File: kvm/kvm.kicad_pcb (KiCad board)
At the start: 2 copper layers, 3 parts, among them U1 FSUSB42MUX, U2 LTC4412xS6, U4 L78L33_SOT89

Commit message: finished schematic
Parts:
- added C1: 100n, Capacitor_SMD:C_0603_1608Metric_Pad1.08x0.95mm_HandSolder, F.Cu at (158.6, 75.0)
- added C10: 100u, Capacitor_THT:CP_Radial_D5.0mm_P2.00mm, F.Cu at (95.9, 17.8)
- added C11: 100u, Capacitor_THT:CP_Radial_D5.0mm_P2.00mm, F.Cu at (103.6, 17.8)
- added C12: 100u, Capacitor_THT:CP_Radial_D5.0mm_P2.00mm, F.Cu at (88.3, 17.8)
- added C13: 100n, Capacitor_SMD:C_0603_1608Metric_Pad1.08x0.95mm_HandSolder, F.Cu at (152.1, 82.7)
- added C14: 100n, Capacitor_SMD:C_0603_1608Metric_Pad1.08x0.95mm_HandSolder, F.Cu at (172.0, 56.0)
- added C15: 100n, Capacitor_SMD:C_0603_1608Metric_Pad1.08x0.95mm_HandSolder, F.Cu at (141.8, 82.9)
- added C16: 100n, Capacitor_SMD:C_0603_1608Metric_Pad1.08x0.95mm_HandSolder, F.Cu at (168.4, 65.9)
- added C17: 100n, Capacitor_SMD:C_0603_1608Metric_Pad1.08x0.95mm_HandSolder, F.Cu at (150.6, 87.8)
- added C18: 100n, Capacitor_SMD:C_0603_1608Metric_Pad1.08x0.95mm_HandSolder, F.Cu at (180.7, 54.4)
- added C19: 100n, Capacitor_SMD:C_0603_1608Metric_Pad1.08x0.95mm_HandSolder, F.Cu at (146.3, 87.8)
- added C2: 100u, Capacitor_THT:CP_Radial_D5.0mm_P2.00mm, F.Cu at (70.5, 17.8)
- added C20: 100n, Capacitor_SMD:C_0603_1608Metric_Pad1.08x0.95mm_HandSolder, F.Cu at (172.0, 58.5)
- added C21: 10u, Capacitor_SMD:C_0805_2012Metric_Pad1.18x1.45mm_HandSolder, F.Cu at (167.1, 60.7)
- added C3: 100n, Capacitor_SMD:C_0603_1608Metric_Pad1.08x0.95mm_HandSolder, F.Cu at (147.8, 82.7)
- added C4: 100n, Capacitor_SMD:C_0603_1608Metric_Pad1.08x0.95mm_HandSolder, F.Cu at (164.0, 65.9)
- added C5: 100n, Capacitor_SMD:C_0603_1608Metric_Pad1.08x0.95mm_HandSolder, F.Cu at (158.6, 72.5)
- added C6: 33p, Capacitor_SMD:C_0603_1608Metric_Pad1.08x0.95mm_HandSolder, F.Cu at (179.7, 49.4)
- added C7: 33p, Capacitor_SMD:C_0603_1608Metric_Pad1.08x0.95mm_HandSolder, F.Cu at (168.4, 63.4)
- added C8: 100n, Capacitor_SMD:C_0603_1608Metric_Pad1.08x0.95mm_HandSolder, F.Cu at (146.3, 85.2)
- added C9: 100u, Capacitor_THT:CP_Radial_D5.0mm_P2.00mm, F.Cu at (78.7, 17.8)
- added D1: D_Schottky, Diode_SMD:D_SOD-123F, F.Cu at (165.1, 48.3)
- added D2: LED, LED_SMD:LED_0805_2012Metric_Pad1.15x1.40mm_HandSolder, F.Cu at (156.5, 48.3)
- added F1: Polyfuse, Fuse:Fuse_1206_3216Metric_Pad1.42x1.75mm_HandSolder, F.Cu at (142.6, 80.0)
- added F2: Polyfuse, Fuse:Fuse_1206_3216Metric_Pad1.42x1.75mm_HandSolder, F.Cu at (136.0, 86.5)
- added F3: Polyfuse, Fuse:Fuse_1206_3216Metric_Pad1.42x1.75mm_HandSolder, F.Cu at (158.9, 61.9)
- added F4: Polyfuse, Fuse:Fuse_1206_3216Metric_Pad1.42x1.75mm_HandSolder, F.Cu at (158.9, 65.2)
- added J1: USB_C_Receptacle_USB2.0, Connector_USB:USB_C_Receptacle_GCT_USB4085, F.Cu at (95.0, 89.0)
- added J2: USB_C_Receptacle_USB2.0, Connector_USB:USB_C_Receptacle_GCT_USB4085, F.Cu at (95.0, 102.0)
- added J3: USB_A_Stacked, Connector_USB:USB_A_Wuerth_61400826021_Horizontal_Stacked, F.Cu at (32.3, 67.6)
- added J4: USB_A_Stacked, Connector_USB:USB_A_Wuerth_61400826021_Horizontal_Stacked, F.Cu at (32.1, 87.1)
- added L1: 600, Resistor_SMD:R_0603_1608Metric_Pad0.98x0.95mm_HandSolder, F.Cu at (168.1, 68.5)
- added L2: 600, Resistor_SMD:R_0603_1608Metric_Pad0.98x0.95mm_HandSolder, F.Cu at (152.1, 80.2)
- added L3: 600, Resistor_SMD:R_0603_1608Metric_Pad0.98x0.95mm_HandSolder, F.Cu at (162.6, 81.3)
- added L4: 600, Resistor_SMD:R_0603_1608Metric_Pad0.98x0.95mm_HandSolder, F.Cu at (179.7, 51.9)
- added L5: 600, Resistor_SMD:R_0603_1608Metric_Pad0.98x0.95mm_HandSolder, F.Cu at (150.6, 85.2)
- added L6: 600, Resistor_SMD:R_0603_1608Metric_Pad0.98x0.95mm_HandSolder, F.Cu at (184.0, 49.4)
- added L7: 600, Resistor_SMD:R_0603_1608Metric_Pad0.98x0.95mm_HandSolder, F.Cu at (163.7, 68.5)
- added Q1: Q_PMOS_GSD, Package_TO_SOT_SMD:SOT-23-3, F.Cu at (50.8, 30.5)
- added R1: 1M, Resistor_SMD:R_0603_1608Metric_Pad0.98x0.95mm_HandSolder, F.Cu at (176.3, 58.3)
- added R10: 10K, Resistor_SMD:R_0603_1608Metric_Pad0.98x0.95mm_HandSolder, F.Cu at (172.7, 61.0)
- added R11: 47K, Resistor_SMD:R_0603_1608Metric_Pad0.98x0.95mm_HandSolder, F.Cu at (162.9, 73.5)
- added R12: 100k, Resistor_SMD:R_0603_1608Metric_Pad0.98x0.95mm_HandSolder, F.Cu at (147.8, 80.2)
- added R13: 780, Resistor_SMD:R_0603_1608Metric_Pad0.98x0.95mm_HandSolder, F.Cu at (147.8, 77.7)
- added R14: 470K, Resistor_SMD:R_0603_1608Metric_Pad0.98x0.95mm_HandSolder, F.Cu at (188.0, 58.4)
- added R2: 1M, Resistor_SMD:R_0603_1608Metric_Pad0.98x0.95mm_HandSolder, F.Cu at (172.7, 63.5)
- added R3: 5.11K, Resistor_SMD:R_0603_1608Metric_Pad0.98x0.95mm_HandSolder, F.Cu at (176.3, 55.8)
- added R4: 5.11K, Resistor_SMD:R_0603_1608Metric_Pad0.98x0.95mm_HandSolder, F.Cu at (163.7, 71.0)
- added R5: 5.11K, Resistor_SMD:R_0603_1608Metric_Pad0.98x0.95mm_HandSolder, F.Cu at (152.1, 77.7)
- added R6: 5.11K, Resistor_SMD:R_0603_1608Metric_Pad0.98x0.95mm_HandSolder, F.Cu at (180.7, 57.0)
- added R7: 680, Resistor_SMD:R_0603_1608Metric_Pad0.98x0.95mm_HandSolder, F.Cu at (184.0, 51.9)
- added R8: 10K, Resistor_SMD:R_0603_1608Metric_Pad0.98x0.95mm_HandSolder, F.Cu at (164.0, 63.4)
- added R9: 20K, Resistor_SMD:R_0603_1608Metric_Pad0.98x0.95mm_HandSolder, F.Cu at (156.5, 80.0)
- added SW1: SW_DPDT_x2, Connector_PinHeader_2.54mm:PinHeader_1x03_P2.54mm_Vertical, F.Cu at (146.9, 62.5)
- added U3: GL850G, Package_SO:SSOP-28_5.3x10.2mm_P0.65mm, F.Cu at (43.2, 50.8)
- added U5: SRV05-4, Package_TO_SOT_SMD:SOT-23-6, F.Cu at (58.4, 38.1)
- added U6: SRV05-4, Package_TO_SOT_SMD:SOT-23-6, F.Cu at (41.8, 38.1)
- added Y1: Crystal, Library:ECS120184XCKM, F.Cu at (55.3, 20.3)
- U4: value L78L33_SOT89 -> SRV05-4; footprint Package_TO_SOT_SMD:SOT-89-3 -> Package_TO_SOT_SMD:SOT-23-6
- moved U2 41.2 mm to (70.7, 37.9)
- moved U4 38.1 mm to (50.8, 38.1)
- moved U1 38.1 mm to (83.8, 38.1)
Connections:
- U1 pad 1: unconnected-(U1-Pad1) -> V5
- U1 pad 10: unconnected-(U1-Pad10) -> GND
- U1 pad 2: unconnected-(U1-Pad2) -> Net-(SW1-Pad2)
- U1 pad 3: unconnected-(U1-Pad3) -> DP0
- U1 pad 4: unconnected-(U1-Pad4) -> DM0
- U1 pad 5: unconnected-(U1-Pad5) -> GND
- U1 pad 6: unconnected-(U1-Pad6) -> DM1IN
- U1 pad 7: unconnected-(U1-Pad7) -> DP1IN
- U1 pad 8: unconnected-(U1-Pad8) -> DM2IN
- U1 pad 9: unconnected-(U1-Pad9) -> DP2IN
- U2 pad 1: unconnected-(U2-Pad1) -> USB2V5
- U2 pad 2: unconnected-(U2-Pad2) -> GND
- U2 pad 3: unconnected-(U2-Pad3) -> GND
- U2 pad 4: unconnected-(U2-Pad4) -> Net-(U2-Pad4)
- U2 pad 5: unconnected-(U2-Pad5) -> /gate
- U2 pad 6: unconnected-(U2-Pad6) -> V5
- U4 pad 1: unconnected-(U4-Pad1) -> DP1
- U4 pad 2: unconnected-(U4-Pad2) -> GND
- U4 pad 3: unconnected-(U4-Pad3) -> DM1

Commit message: first layout version
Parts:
- moved L6 117.2 mm to (76.7, 96.7), turned to 180 degrees
- moved C18 114.3 mm to (76.8, 102.0), turned to -90 degrees
- moved C2 113.5 mm to (144.1, 104.2), turned to -90 degrees
- moved Q1 111.4 mm to (135.5, 102.9), turned to 90 degrees
- moved Y1 106.9 mm to (111.4, 111.4), turned to 180 degrees
- moved L4 105.6 mm to (77.2, 77.3), turned to 180 degrees
- moved U5 97.5 mm to (143.9, 85.1), turned to 90 degrees
- moved U2 96.3 mm to (135.8, 109.0), turned to 180 degrees
- moved R7 93.9 mm to (101.2, 96.3), turned to 180 degrees
- moved C16 92.4 mm to (77.2, 80.4), turned to -90 degrees
- moved C6 88.4 mm to (112.2, 106.6), turned to 180 degrees
- moved C11 86.5 mm to (84.9, 102.2), turned to 90 degrees
- moved U6 85.6 mm to (87.4, 110.5)
- moved L3 82.3 mm to (80.3, 81.3)
- moved U3 79.2 mm to (109.0, 94.8), turned to 90 degrees
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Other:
- copper layers 2 -> 4

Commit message: first pcb layout
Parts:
- moved J1 105.8 mm to (66.1, 46.7), turned to -90 degrees
- moved R4 102.6 mm to (64.5, 57.1), turned to -90 degrees
- moved D1 102.2 mm to (75.3, 42.9), turned to 180 degrees
- moved R6 99.2 mm to (71.6, 46.8), turned to 90 degrees
- moved R3 99.1 mm to (69.5, 46.8), turned to 90 degrees
- moved L1 97.6 mm to (70.6, 42.9)
- moved R5 95.6 mm to (67.4, 57.1), turned to 90 degrees
- moved J2 93.7 mm to (66.1, 61.4), turned to -90 degrees
- moved R1 89.8 mm to (70.0, 57.1), turned to 90 degrees
- moved C3 87.0 mm to (77.7, 48.0)
- moved R10 84.3 mm to (69.8, 67.4), turned to 0 degrees
- moved U3 84.2 mm to (83.8, 42.7), turned to 0 degrees
- moved C1 80.6 mm to (81.9, 48.9)
- moved R2 78.1 mm to (84.1, 45.7)
- moved L2 74.8 mm to (82.5, 54.0)
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- renumbered C3 to C1, C5 to C10, C4 to C11, C20 to C12, C8 to C13, C18 to C14, C19 to C15, C12 to C16, C11 to C17, C6 to C18, C13 to C19, C1 to C2, C7 to C20, C14 to C21, C2 to C3, C10 to C4, C17 to C5, C9 to C6, C16 to C7, C15 to C8, C21 to C9, F2 to F1, F1 to F2, F4 to F3, F3 to F4, L7 to L5, L5 to L7, R6 to R1, R4 to R10, R7 to R11, R10 to R13, R11 to R14, R14 to R2, R5 to R3, R1 to R4, R2 to R5, R3 to R6, R8 to R7, R9 to R8, R13 to R9, U5 to U2, U2 to U3, U3 to U4, U4 to U5
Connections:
- net DM0 renamed D0-
- net DM1 renamed D1-
- net DM1IN renamed D1IN-
- net DM2 renamed D2-
- net DM2IN renamed D2IN-
- net DM3 renamed D3-
- net DM4 renamed D4-
- net DP0 renamed D0+
- net DP1 renamed D1+
- net DP1IN renamed D1IN+
- net DP2 renamed D2+
- net DP2IN renamed D2IN+
- net DP3 renamed D3+
- net DP4 renamed D4+
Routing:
- net D4+: track 0.00 -> 73.8 mm, vias 0 -> 2
- net D4-: track 0.00 -> 67.5 mm
- net GND: track 0.00 -> 64.6 mm, vias 0 -> 30
- net D3+: track 0.00 -> 59.5 mm, vias 0 -> 2
- net V5: track 0.00 -> 59.4 mm, vias 0 -> 19
- net D3-: track 0.00 -> 58.1 mm, vias 0 -> 2
- net D2-: track 0.00 -> 44.0 mm
- net D2+: track 0.00 -> 42.0 mm, vias 0 -> 2
- net D1-: track 0.00 -> 39.5 mm, vias 0 -> 2
- net DVDD: track 0.00 -> 37.1 mm
- net AVDD: track 0.00 -> 36.1 mm, vias 0 -> 3
- net D1+: track 0.00 -> 34.1 mm
- net D2IN+: track 0.00 -> 31.8 mm, vias 0 -> 2
- net D2IN-: track 0.00 -> 29.5 mm, vias 0 -> 2
- net Net-(J2-PadA4): track 0.00 -> 28.4 mm, vias 0 -> 1
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- added copper zone on In1.Cu, net GND
- added copper zone on In2.Cu, net V5
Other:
- board text added: "K(V)M - USB Hub"
- board text added: "V01"

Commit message: small layout changes
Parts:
- moved J3 0.22 mm to (74.8, 76.1)
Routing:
- net V5: track 59.4 -> 48.2 mm, vias 19 -> 15
- net D2+: track 42.0 -> 46.4 mm
- net D1-: track 39.5 -> 42.0 mm
- net D2-: track 44.0 -> 45.9 mm
- net D1+: track 34.1 -> 35.1 mm

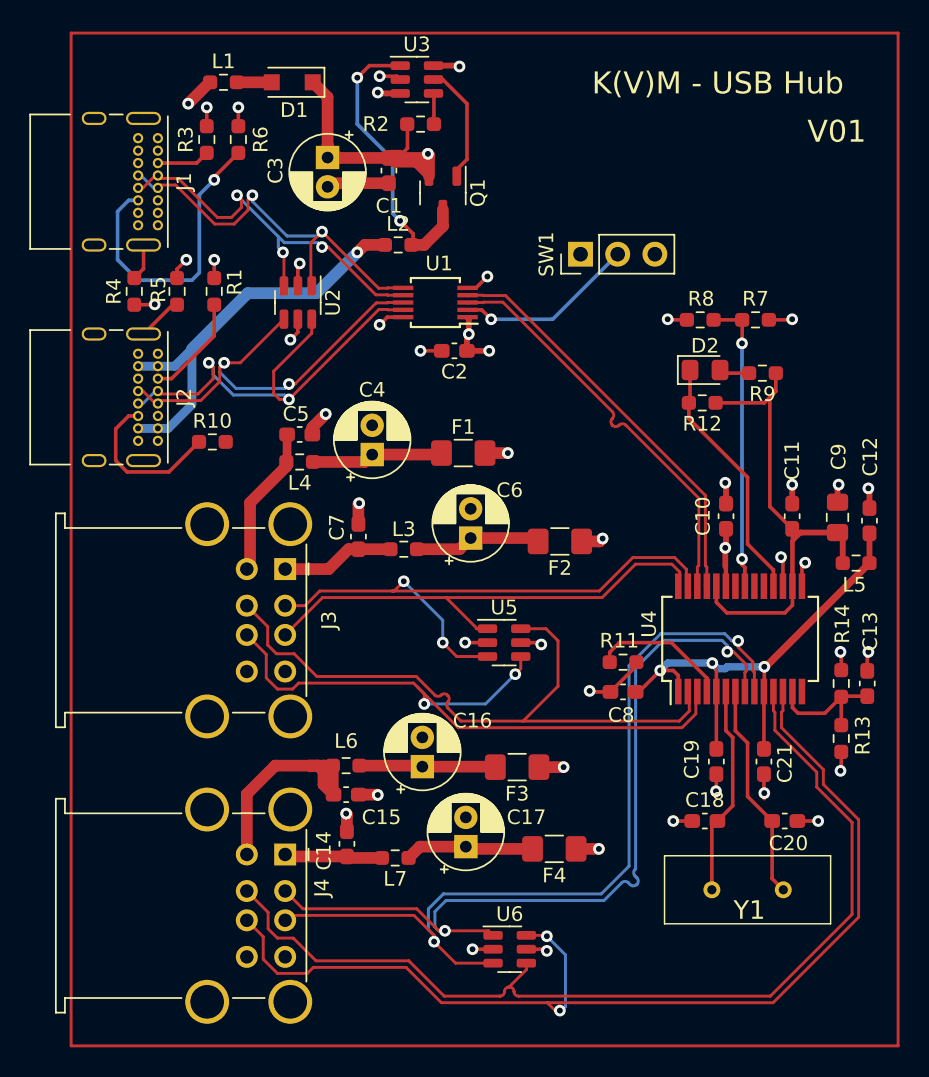
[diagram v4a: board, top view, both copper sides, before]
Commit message: replaced USB-C ports with smd parts
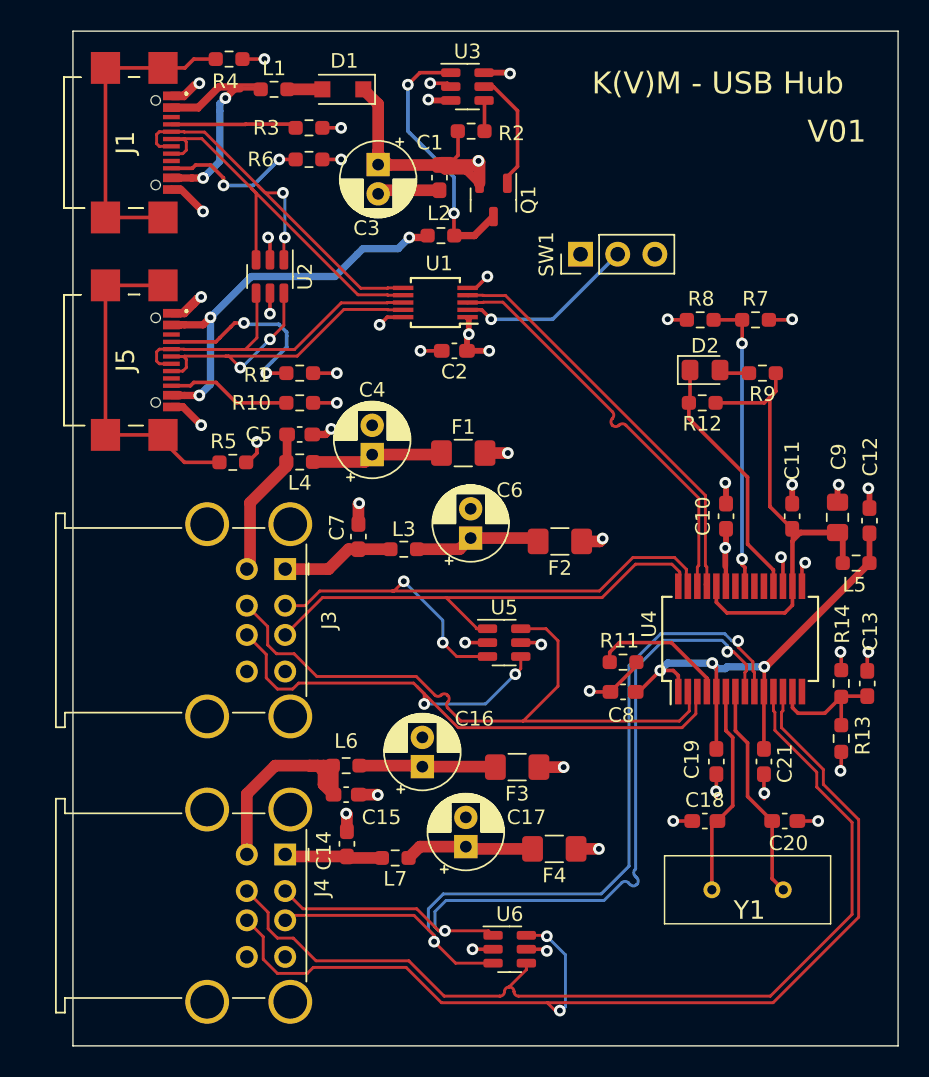
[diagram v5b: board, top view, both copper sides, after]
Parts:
- removed J2: USB_C_Receptacle_USB2.0, Connector_USB:USB_C_Receptacle_GCT_USB4085
- added J5: USB4110-GF-A, Library:USB4110GFA, F.Cu at (63.4, 61.8)
- J1: value USB_C_Receptacle_USB2.0 -> USB4110-GF-A; footprint Connector_USB:USB_C_Receptacle_GCT_USB4085 -> Library:USB4110GFA
- moved R4 17.1 mm to (71.0, 41.3), turned to 0 degrees
- moved R5 12.3 mm to (71.2, 68.8), turned to 0 degrees
- moved R1 8.08 mm to (75.8, 62.7), turned to 0 degrees
- moved R3 7.03 mm to (76.5, 46.0), turned to 0 degrees
- moved R10 6.54 mm to (75.8, 64.8)
- moved R6 5.01 mm to (76.5, 48.1), turned to 0 degrees
- moved L1 3.49 mm to (74.1, 43.3)
- moved Q1 3.49 mm to (89.1, 50.9)
- moved R2 3.49 mm to (87.5, 46.2)
- moved C1 3.49 mm to (85.4, 49.4)
- moved C3 3.49 mm to (81.2, 48.5)
- moved U3 3.49 mm to (87.3, 43.2)
- moved D1 3.49 mm to (78.8, 43.3)
- moved L2 2.99 mm to (85.5, 53.3)
- moved J1 2.77 mm to (63.4, 47.0)
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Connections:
- net Net-(J1-PadA4) renamed USB1VBUS
- L2 pad 1: Net-(J2-PadA4) -> USB2VBUS
- R4 pad 1: Net-(J1-PadS1) -> Net-(J1-PadMP1)
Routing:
- net USB2VBUS: track 0.00 -> 29.4 mm, vias 0 -> 3
- net Net-(J2-PadA4): track 28.4 -> 0.00 mm, vias 1 -> 0
- net Net-(J1-PadMP1): track 0.00 -> 21.9 mm
- net Net-(J5-PadMP1): track 3.12 -> 23.0 mm
- net Net-(J1-PadB5): track 20.7 -> 10.2 mm, vias 1 -> 2
- net USB1VBUS: track 18.4 -> 28.0 mm, vias 1 -> 2
- net Net-(J5-PadA5): track 7.19 -> 13.4 mm, vias 0 -> 2
- net D2IN-: track 29.5 -> 24.4 mm, vias 2 -> 0
- net Net-(J1-PadA5): track 3.63 -> 8.60 mm
- net GND: track 64.6 -> 69.0 mm, vias 30 -> 35
- net D2IN+: track 31.8 -> 27.7 mm
- net Net-(J1-PadS1): track 2.52 -> 0.00 mm
- net Net-(J5-PadB5): track 10.9 -> 8.53 mm
- net USB2V5: track 20.1 -> 18.1 mm
- net D1IN-: track 28.3 -> 29.7 mm
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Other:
- board outline added: 56.4 x 69.3 mm

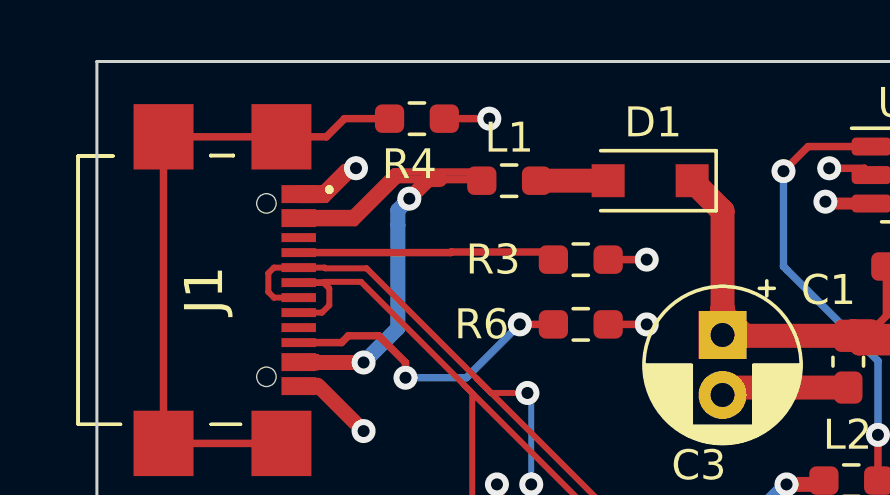
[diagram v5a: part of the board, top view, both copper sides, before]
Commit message: updated layout
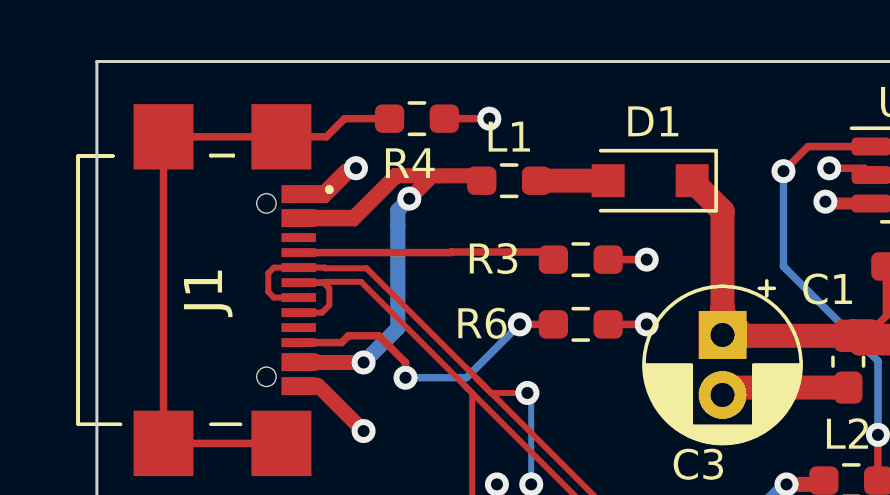
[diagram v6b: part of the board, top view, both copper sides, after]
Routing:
- net USB1VBUS: track 28.0 -> 30.5 mm
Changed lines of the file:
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@@
   (segment (start 67.051 49.54) (end 67.681 49.54) (width 0.25) (layer "F.Cu") (net 51))
   (segment (start 67.691 44.577) (end 68.834 44.577) (width 0.25) (layer "F.Cu") (net 51))
+  (segment (start 70.485 43.18) (end 70.358 43.307) (width 0.25) (layer "F.Cu") (net 51))
   (segment (start 70.739 43.942) (end 71.374 43.307) (width 0.5) (layer "F.Cu") (net 51))
   (segment (start 68.925 44.74) (end 70.358 43.307) (width 0.25) (layer "F.Cu") (net 51))
@@
   (segment (start 67.681 49.54) (end 67.691 49.53) (width 0.25) (layer "F.Cu") (net 51))
   (segment (start 71.755 43.307) (end 73.119092 43.307) (width 0.25) (layer "F.Cu") (net 51))
+  (segment (start 72.992092 43.18) (end 70.485 43.18) (width 0.25) (layer "F.Cu") (net 51))
   (segment (start 68.834 44.577) (end 70.358 43.053) (width 0.25) (layer "F.Cu") (net 51))
   (segment (start 67.691 49.276) (end 67.655 49.24) (width 0.25) (layer "F.Cu") (net 51))
   (segment (start 73.155 43.342908) (end 73.116092 43.342908) (width 0.8) (layer "F.Cu") (net 51))
   (segment (start 67.528 44.74) (end 67.691 44.577) (width 0.25) (layer "F.Cu") (net 51))
-  (segment (start 71.374 43.307) (end 71.755 43.307) (width 0.5) (layer "F.Cu") (net 51))
   (segment (start 68.844 44.44) (end 70.231 43.053) (width 0.25) (layer "F.Cu") (net 51))
   (segment (start 67.691 49.53) (end 67.691 49.403) (width 0.25) (layer "F.Cu") (net 51))
@@
   (segment (start 67.051 44.74) (end 67.528 44.74) (width 0.25) (layer "F.Cu") (net 51))
   (segment (start 70.358 43.053) (end 72.865092 43.053) (width 0.25) (layer "F.Cu") (net 51))
+  (segment (start 73.155 43.342908) (end 72.992092 43.18) (width 0.25) (layer "F.Cu") (net 51))
   (via (at 69.215 49.403) (size 0.8) (drill 0.4) (layers "F.Cu" "B.Cu") (net 51))
   (via (at 70.739 43.942) (size 0.8) (drill 0.4) (layers "F.Cu" "B.Cu") (net 51))

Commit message: reanotated on pcb
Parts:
- renumbered C3 to C1, C9 to C10, C8 to C11, C16 to C15, C17 to C16, C15 to C17, C19 to C18, C18 to C19, C1 to C3, C7 to C4, C4 to C6, C6 to C7, C10 to C8, C11 to C9, J5 to J1, J1 to J2, L7 to L6, L6 to L7, R5 to R10, R12 to R11, R11 to R12, R3 to R2, R2 to R3, R6 to R4, R4 to R5, R7 to R6, R8 to R7, R9 to R8, R10 to R9, U2 to U1, U3 to U2, U1 to U3
